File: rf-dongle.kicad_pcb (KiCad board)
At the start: 2 copper layers, 36 parts, among them J1 USB_A, J2 Conn_01x05_Socket, SW1 SW_Push, SW2 SW_Push, U1 nRF52840-QIXX, X1 32MHz, X2 32.768kHz

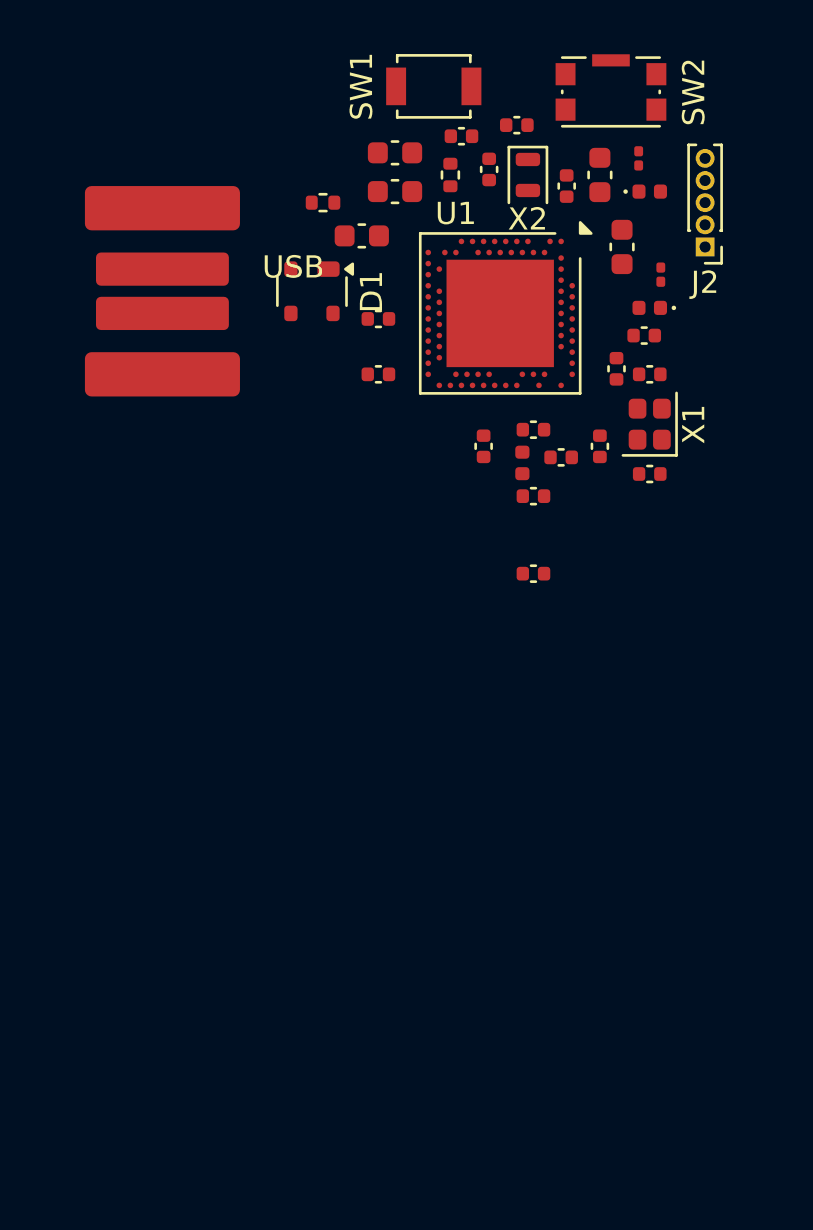
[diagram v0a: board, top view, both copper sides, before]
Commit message: setup pcb stackup
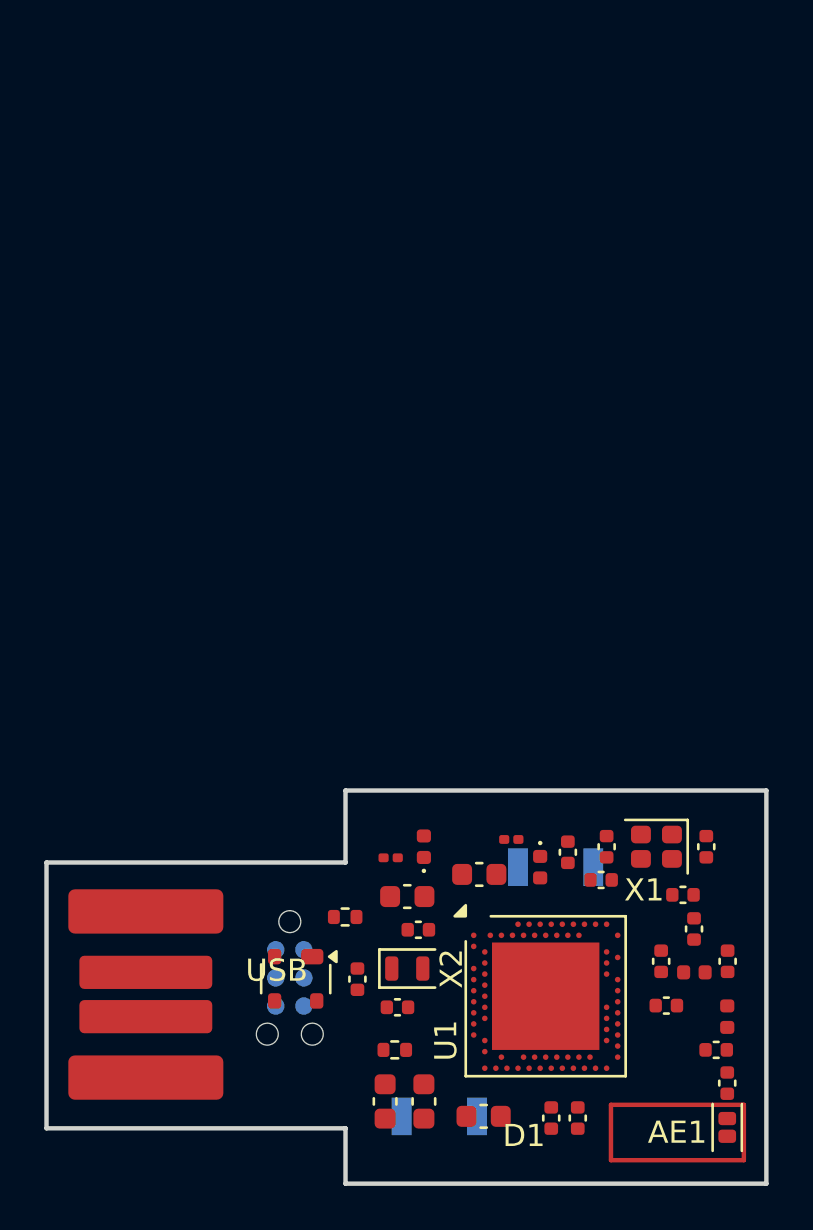
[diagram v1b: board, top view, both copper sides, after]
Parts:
- removed C23: 100nF, Capacitor_SMD:C_0402_1005Metric
- removed J2: Conn_01x05_Socket, Connector_PinHeader_1.00mm:PinHeader_1x05_P1.00mm_Vertical
- added AE1: Antenna_Chip, Inductor_SMD:L_TDK_MLZ1608, F.Cu at (147.0, 153.0)
- added J3: TC2030, Connector:Tag-Connect_TC2030-IDC-NL_2x03_P1.27mm_Vertical, B.Cu at (127.2, 146.2)
- added Z2: 3.9nH, Inductor_SMD:L_0402_1005Metric, F.Cu at (147.0, 148.0)
- added Z3: N.C, Capacitor_SMD:C_0402_1005Metric, F.Cu at (146.5, 149.5)
- SW1: moved to B.Cu
- SW2: footprint Button_Switch_SMD:SW_Push_1P1T-SH_NO_CK_KMR2xxG -> Button_Switch_SMD:SW_SPST_B3U-1000P; moved to B.Cu
- moved SW1 46.5 mm to (134.0, 152.5)
- moved C6 42.8 mm to (131.6, 151.8), turned to 90 degrees
- moved C19 41.1 mm to (133.3, 151.8), turned to 90 degrees
- moved C20 40.1 mm to (136.0, 152.5)
- moved R2 39.6 mm to (132.0, 149.5), turned to 0 degrees
- moved C17 39.2 mm to (130.3, 146.3), turned to 90 degrees
- moved C18 38.1 mm to (132.1, 147.6), turned to 180 degrees
- moved C7 36.9 mm to (139.1, 152.6), turned to 90 degrees
- moved X2 36.2 mm to (132.6, 145.8), turned to 0 degrees
- moved SW2 35.1 mm to (139.2, 141.2), turned to 180 degrees
- moved C8 34.8 mm to (140.2, 152.6), turned to 90 degrees
- moved C5 34.2 mm to (133.1, 144.1), turned to 180 degrees
- moved C14 33.7 mm to (132.6, 142.6), turned to 0 degrees
- moved R4 33.5 mm to (131.8, 140.8), turned to 0 degrees
- moved R1 32.3 mm to (129.8, 143.5)
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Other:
- board outline added: 32.5 x 17.8 mm
- copper layers 2 -> 4

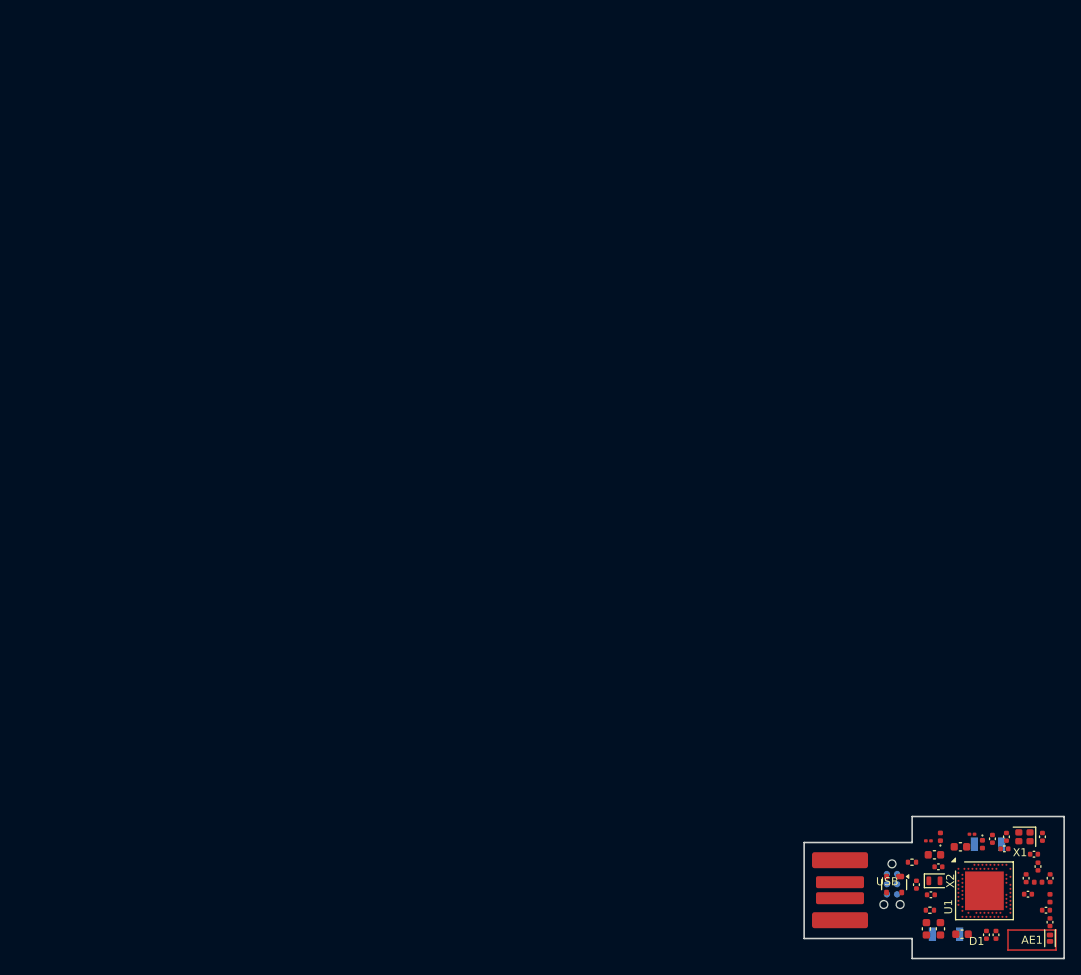
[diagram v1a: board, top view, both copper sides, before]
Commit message: setup constraints, first attempt at routing
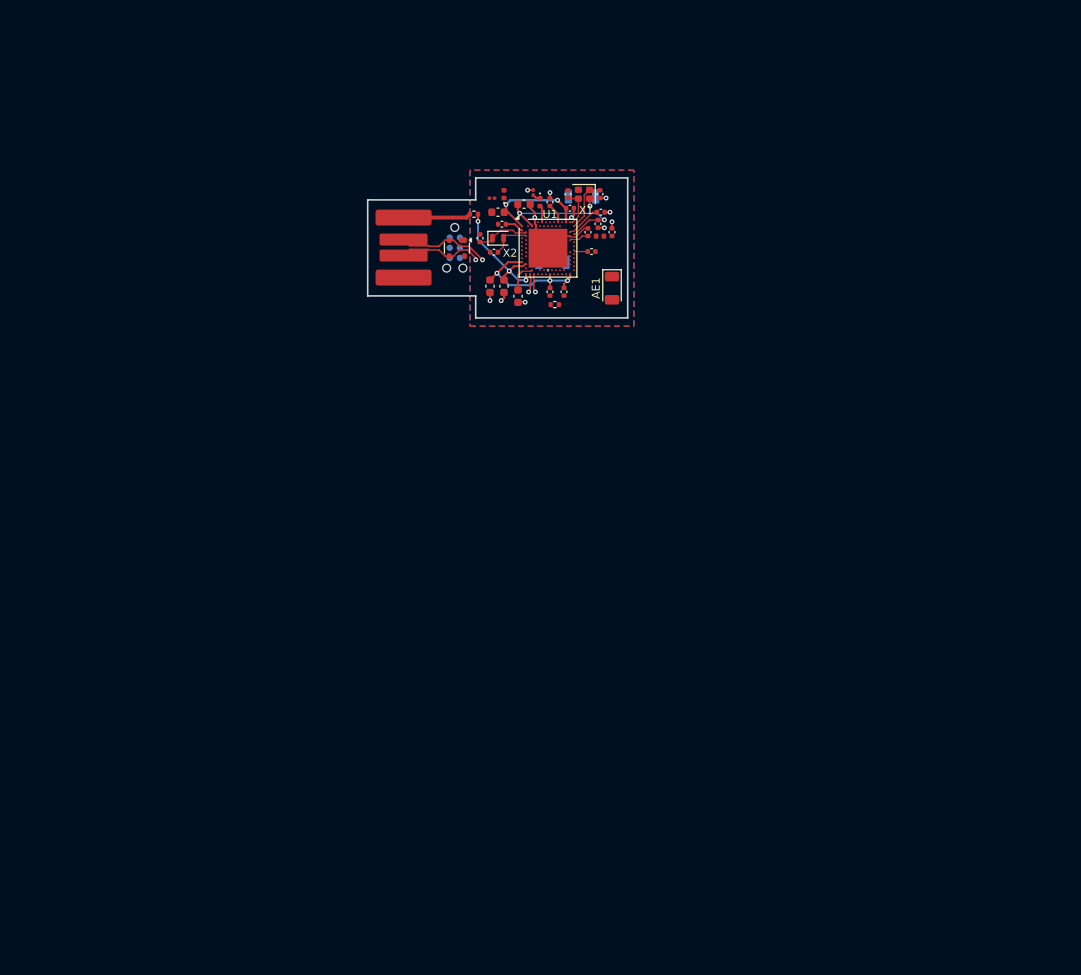
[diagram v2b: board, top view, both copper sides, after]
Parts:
- removed C22: N.C., Capacitor_SMD:C_0402_1005Metric
- removed Z2: 3.9nH, Inductor_SMD:L_0402_1005Metric
- removed Z3: N.C, Capacitor_SMD:C_0402_1005Metric
- AE1: footprint Inductor_SMD:L_TDK_MLZ1608 -> RF_Antenna:Johanson_2450AT18x100
- moved AE1 98.0 mm to (92.2, 71.8)
- moved R1 97.8 mm to (75.0, 62.5)
- moved C3 97.6 mm to (89.2, 64.8)
- moved C4 97.6 mm to (92.2, 64.8)
- moved L1 97.6 mm to (90.8, 65.2)
- moved C1 97.5 mm to (90.8, 60.0)
- moved C17 97.5 mm to (75.8, 65.5), turned to -90 degrees
- moved D2 97.5 mm to (83.2, 61.0)
- moved X1 97.4 mm to (88.8, 60.0)
- moved C10 97.4 mm to (90.5, 63.7)
- moved SW1 97.3 mm to (84.8, 68.5), turned to 0 degrees
- moved C2 97.2 mm to (86.8, 60.0)
- moved R3 97.2 mm to (82.4, 59.8), turned to -90 degrees
- moved C20 97.2 mm to (80.5, 72.8), turned to 90 degrees
- moved C7 97.1 mm to (84.5, 72.2)
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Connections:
- net D_M renamed D-
- net D_P renamed D+
- AE1 pad 1: Net-(AE1-FEED) -> /RF
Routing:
- net VEXT: track 0.00 -> 32.3 mm, vias 0 -> 5
- net D+: track 0.00 -> 23.5 mm, vias 0 -> 2
- net D-: track 0.00 -> 22.6 mm, vias 0 -> 2
- net GND: track 0.00 -> 22.4 mm, vias 0 -> 12
- net /DEC4_6: track 0.00 -> 19.0 mm, vias 0 -> 2
- net /VBUS_nRF: track 0.00 -> 15.9 mm, vias 0 -> 3
- net VBUS: track 0.00 -> 8.47 mm
- net /XC1: track 0.00 -> 6.69 mm
- net /XL1: track 0.00 -> 6.55 mm
- net /XL2: track 0.00 -> 5.63 mm
- net /XC2: track 0.00 -> 5.03 mm
- net /DEC3: track 0.00 -> 4.31 mm
- net /DECUSB: track 0.00 -> 3.84 mm
- net Net-(U1-ANT): track 0.00 -> 2.49 mm
- net /DEC2: track 0.00 -> 2.43 mm
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- added copper zone on B.Cu, net GND
- added copper zone on F.Cu, net GND
- added copper zone on In1.Cu, net GND
- added copper zone on In2.Cu, net GND
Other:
- board size 32.5 x 17.8 mm -> 32.5 x 17.5 mm
- board text added: "The PCB stackup is: JLC04161H-3313 Diaelectric constant Prepreg: 4.1 Core FR4: 4.5"
- board text added: "The rectangles around the edges of the board (User.1 layer) are clearance for the dongle's casing."

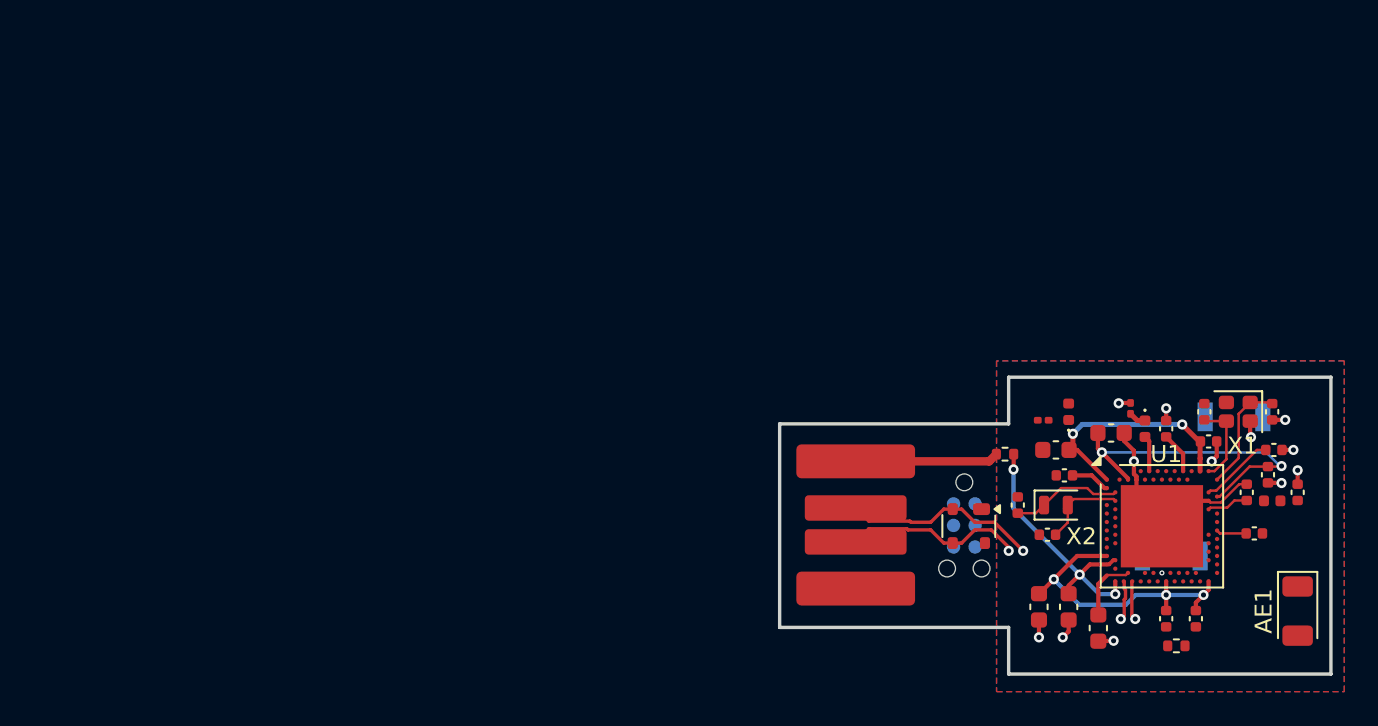
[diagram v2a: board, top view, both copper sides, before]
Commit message: second attempt at routing
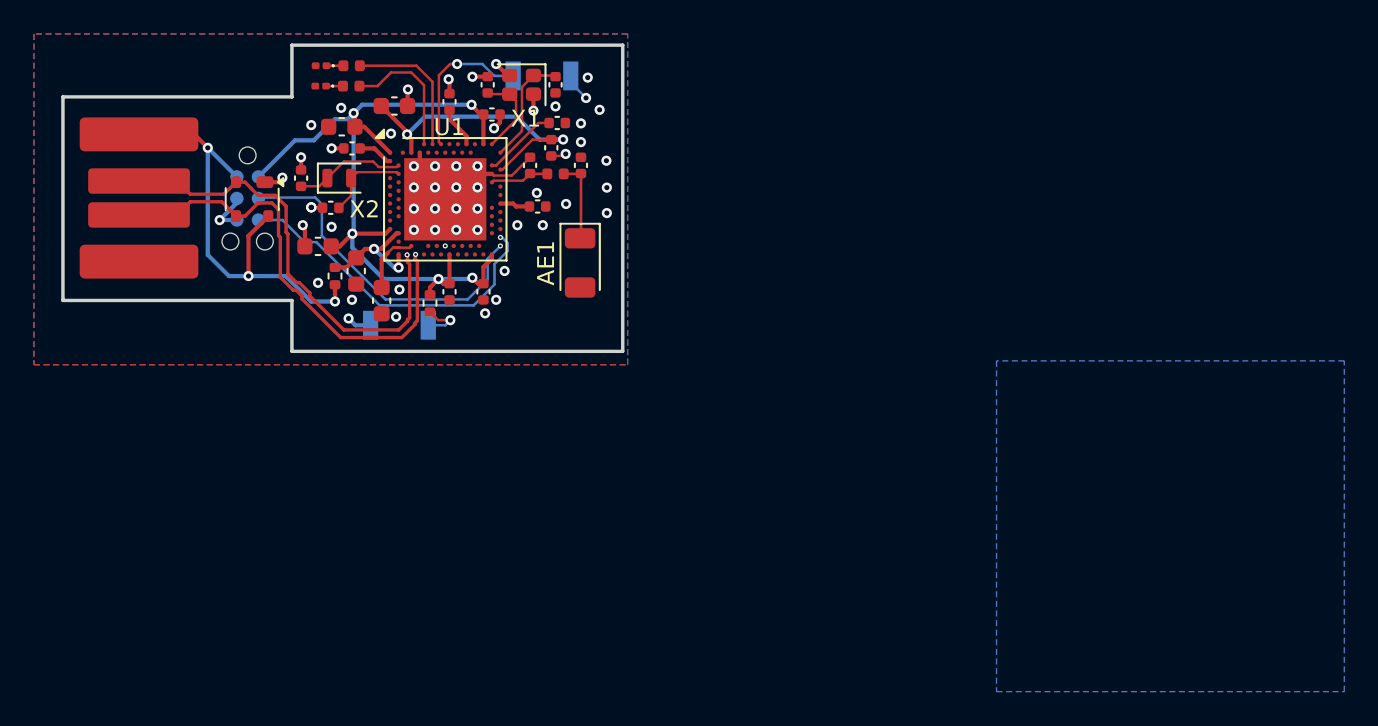
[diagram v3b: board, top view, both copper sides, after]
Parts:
- moved R3 51.8 mm to (34.7, 39.6), turned to 0 degrees
- moved D2 51.4 mm to (36.5, 39.6), turned to 0 degrees
- moved R2 48.4 mm to (41.1, 53.6), turned to -90 degrees
- moved C6 47.5 mm to (34.5, 50.2), turned to 0 degrees
- moved SW1 47.5 mm to (39.3, 54.9)
- moved AE1 47.0 mm to (50.0, 51.2)
- moved R4 46.9 mm to (34.7, 40.8)
- moved C20 46.4 mm to (38.2, 53.5)
- moved D3 46.4 mm to (36.5, 40.8), turned to 0 degrees
- moved C1 46.4 mm to (48.5, 40.7)
- moved C10 46.4 mm to (48.2, 44.4)
- moved C12 46.4 mm to (44.8, 42.5)
- moved C13 46.4 mm to (42.2, 41.7)
- moved C15 46.4 mm to (39.0, 42.0)
- moved C17 46.4 mm to (33.5, 46.2)
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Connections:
- net Net-(U1-ANT) renamed /ANT
- J3 pad 1: GND -> VEXT
- J3 pad 4: VDD_nRF -> GND
- U1 pad A12: unconnected-(U1-P0.02-PadA12) -> BTN_1
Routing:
- net SWDCLK: track 0.00 -> 20.2 mm, vias 0 -> 1
- net SWDIO: track 0.00 -> 19.9 mm, vias 0 -> 1
- net VBUS: track 8.47 -> 26.8 mm, vias 0 -> 3
- net VEXT: track 32.3 -> 46.8 mm
- net BTN_1: track 0.00 -> 9.06 mm, vias 0 -> 1
- net /VBUS_nRF: track 15.9 -> 7.24 mm, vias 3 -> 2
- net RESET: track 0.00 -> 8.15 mm, vias 1 -> 2
- net LED_2: track 0.00 -> 7.93 mm
- net LED_1: track 2.12 -> 8.35 mm
- net /RF: track 0.00 -> 4.61 mm
- net GND: track 22.4 -> 26.6 mm, vias 12 -> 55
- net D-: track 22.6 -> 26.7 mm, vias 2 -> 1
- net D+: track 23.5 -> 27.5 mm, vias 2 -> 1
- net /ANT: track 2.49 -> 3.49 mm
- net Net-(D3-K): track 0.00 -> 0.99 mm
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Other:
- board size 32.5 x 17.5 mm -> 33 x 18 mm
- board text added: "#808080D4"
- board text added: "0"
- board text added: "0 mm"
- board text added: "0.01 mm"
- board text added: "0.0152 mm"
- board text added: "0.02"
- board text added: "0.035 mm"
- board text added: "0.0994 mm"
- board text added: "1"
- board text added: "1.265 mm"
- board text added: "3.3"
- board text added: "4.1"
- board text added: "4.5"
- board text added: "B.Cu"
- board text added: "B.Mask"
- board text added: "B.Paste"
- board text added: "B.Silkscreen"
- board text added: "Bottom Silk Screen"
- board text added: "Bottom Solder Mask"
- board text added: "Bottom Solder Paste"
- board text added: "Color"
- board text added: "Dielectric"
- board text added: "Epsilon R"
- board text added: "F.Cu"
- board text added: "F.Mask"
- board text added: "F.Paste"
- board text added: "F.Silkscreen"
- board text added: "FR4"
- board text added: "In1.Cu"
- board text added: "In2.Cu"
- board text added: "Layer Name"
- board text added: "Loss Tangent"
- board text added: "Material"
- board text added: "Not specified"
- board text added: "Thickness (mm)"
- board text added: "Top Silk Screen"
- board text added: "Top Solder Mask"
- board text added: "Top Solder Paste"
- board text added: "Type"
- board text added: "copper"
- board text added: "core"
- board text added: "prepreg"
